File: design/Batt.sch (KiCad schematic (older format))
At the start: 1 part

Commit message: Renew pdf set some vaules add links and more comments
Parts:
- BT?: Max_voltage (none) -> 4,1; Min_volltage (none) -> 2,8
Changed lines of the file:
@@
 $Descr A4 11693 8268
 encoding utf-8
-Sheet 5 68
+Sheet 37 101
 Title ""
 Date ""
@@
 F 5 "2200mAh" H 5500 3450 60  0001 C CNN "Capacity"
 F 6 "150A" H 5500 3450 60  0001 C CNN "Max_out_current"
+F 7 "4,1" H 5500 3450 60  0001 C CNN "Max_voltage"
+F 8 "2,8" H 5500 3450 60  0001 C CNN "Min_volltage"
 	1    5500 3450
 	1    0    0    -1

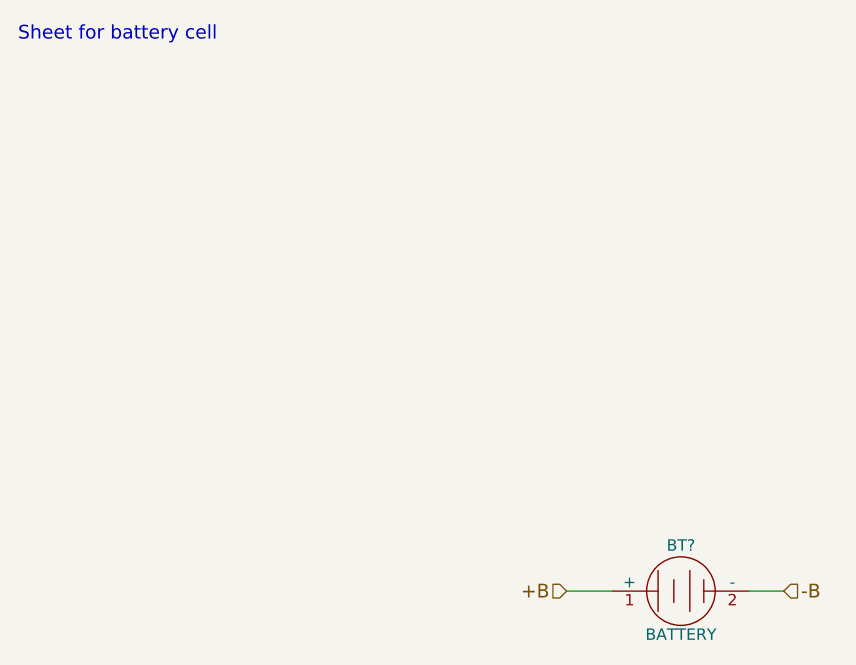
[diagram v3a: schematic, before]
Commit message: Fix schematic so its more readable (I think so)
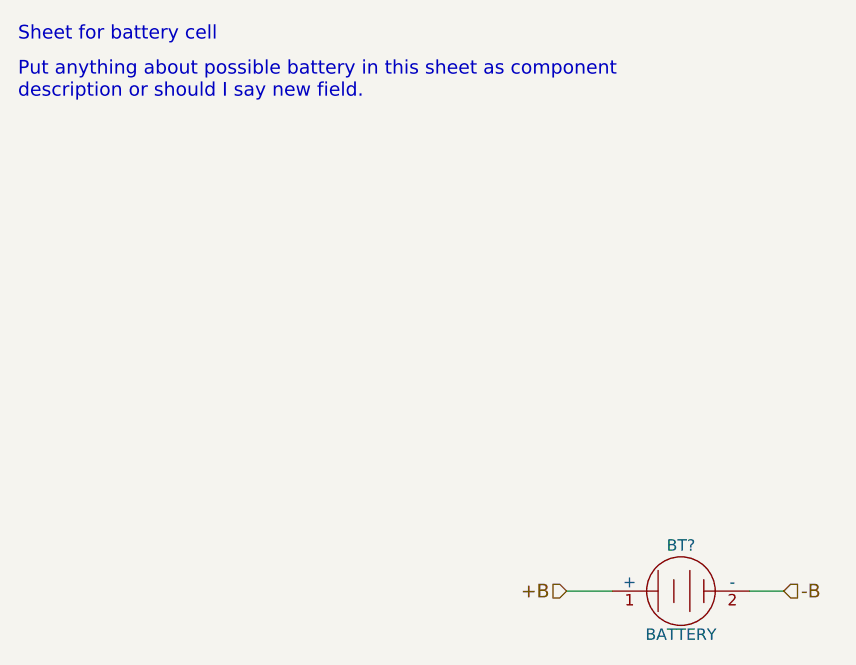
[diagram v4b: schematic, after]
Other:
- note added: "Put anything about possible battery in this sheet as component \ndescription or should I say new field.\n"
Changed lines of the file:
@@
 $Descr A4 11693 8268
 encoding utf-8
-Sheet 37 101
+Sheet 36 101
 Title ""
 Date ""
@@
 Wire Wire Line
 	5800 3450 5950 3450
+Text Notes 2600 1300 0    60   ~ 0
+Put anything about possible battery in this sheet as component \ndescription or should I say new field.\n
 $EndSCHEMATC
